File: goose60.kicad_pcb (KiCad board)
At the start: 2 copper layers, 285 x 94.6 mm, 179 parts, among them J1 Debugger, J2 USART, J3 SPI, P1 USB_C_Plug_USB2.0, SW1 SW_Push, SW10 SW_Push, SW11 SW_Push, SW14 SW_Push, SW15 SW_Push, SW16 SW_Push, SW18 SW_Push, SW2 SW_Push, SW20 SW_Push, SW21 SW_Push, SW22 SW_Push, SW23 SW_Push, SW24 SW_Push, SW25 SW_Push, SW26 SW_Push, SW27 SW_Push, SW28 SW_Push, SW29 SW_Push, SW3 SW_Push, SW30 SW_Push, SW31 SW_Push, SW32 SW_Push, SW35 SW_Push, SW36 SW_Push, SW37 SW_Push, SW38 SW_Push, SW39 SW_Push, SW40 SW_Push, SW41 SW_Push, SW42 SW_Push, SW43 SW_Push, SW44 SW_Push, SW45 SW_Push, SW46 SW_Push, SW47 SW_Push, SW48 SW_Push, SW49 SW_Push, SW5 SW_Push, SW50 SW_Push, SW51 SW_Push, SW52 SW_Push, SW53 SW_Push, SW54 SW_Push, SW56 SW_Push, SW58 SW_Push, SW59 SW_Push, SW60 SW_Push, SW61 SW_Push, SW62 SW_Push, SW65 SW_Push, SW66 SW_Push, SW67 SW_Push, SW68 SW_Push, SW69 SW_Push, SW7 SW_Push, SW71 SW_Push, SW73 SW_Push, SW74 SW_Push, SW75 SW_Push, SW76 SW_Push, SW78 SW_Push, SW79 SW_Push, SW80 SW_Push, SW82 SW_Push, SW84 SW_Push, SW86 SW_Push, SW9 SW_Push, U1 STM32F103CBTx, U2 LM317_SOT-223, X1 Crystal_GND24

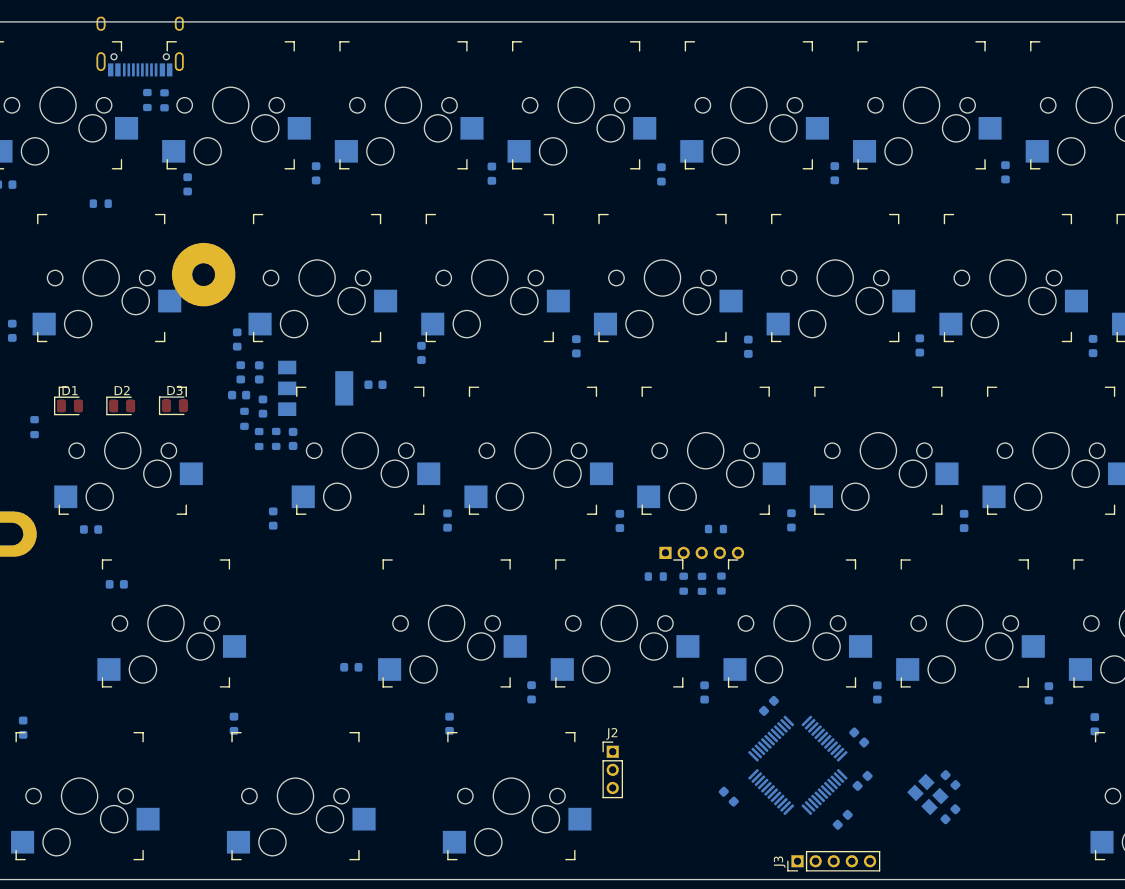
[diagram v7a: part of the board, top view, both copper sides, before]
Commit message: add res and fix rule check fail problom
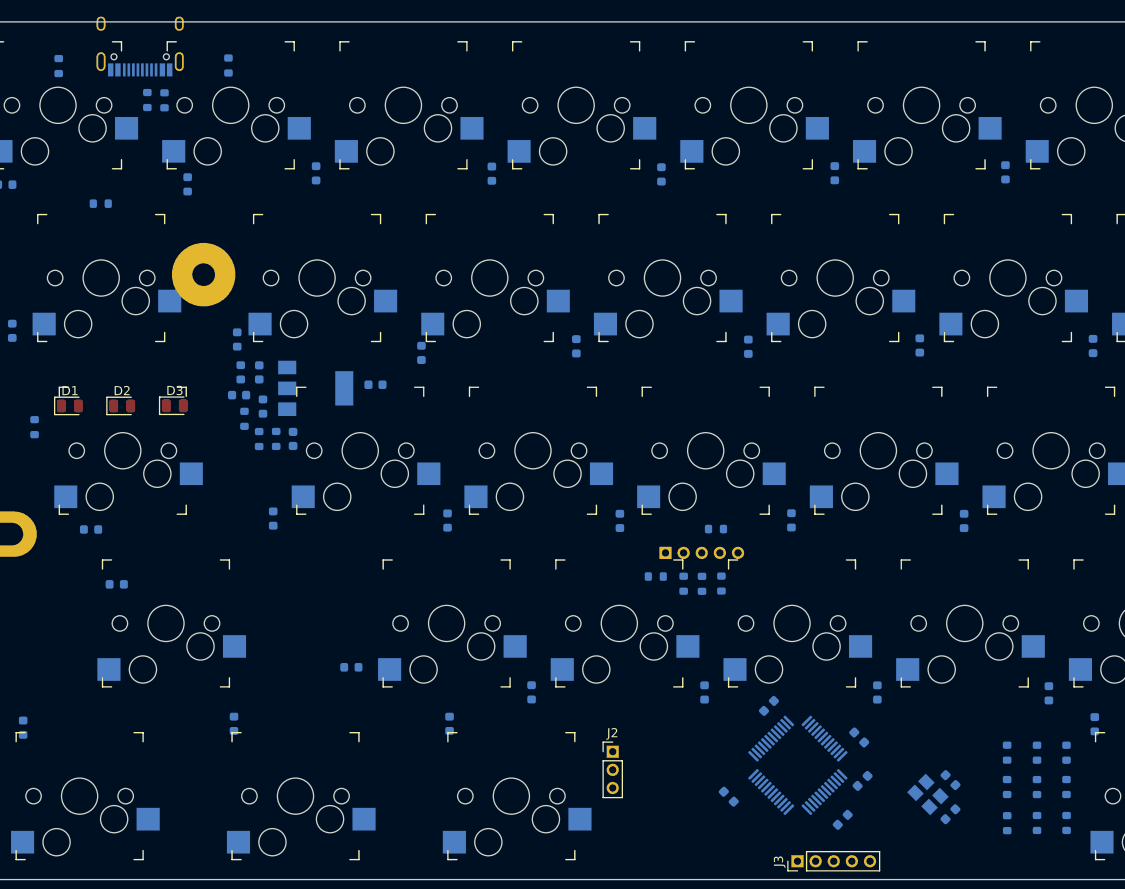
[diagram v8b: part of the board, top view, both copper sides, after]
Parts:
- added R15: 10K, Resistor_SMD:R_0603_1608Metric, B.Cu at (176.4, 145.8)
- added R16: 10K, Resistor_SMD:R_0603_1608Metric, B.Cu at (176.4, 149.6)
- added R17: 10K, Resistor_SMD:R_0603_1608Metric, B.Cu at (179.7, 145.8)
- added R18: 10K, Resistor_SMD:R_0603_1608Metric, B.Cu at (179.7, 149.6)
- added R19: 10K, Resistor_SMD:R_0603_1608Metric, B.Cu at (182.9, 145.8)
- added R20: 10K, Resistor_SMD:R_0603_1608Metric, B.Cu at (182.9, 149.6)
- added R21: 10K, Resistor_SMD:R_0603_1608Metric, B.Cu at (182.9, 153.6)
- added R22: 10K, Resistor_SMD:R_0603_1608Metric, B.Cu at (179.7, 153.6)
- added R23: 10K, Resistor_SMD:R_0603_1608Metric, B.Cu at (176.4, 153.6)
- added R24: 5.1K, Resistor_SMD:R_0603_1608Metric, B.Cu at (71.8, 70.1)
- added R25: 0, Resistor_SMD:R_0603_1608Metric, B.Cu at (90.5, 70.0)
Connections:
- net /col1 renamed col1
- net /col10 renamed col10
- net /col11 renamed col11
- net /col12 renamed col12
- net /col13 renamed col13
- net /col14 renamed col14
- net /col2 renamed col2
- net /col3 renamed col3
- net /col4 renamed col4
- net /col5 renamed col5
- net /col6 renamed col6
- net /col7 renamed col7
- net /col8 renamed col8
- net /col9 renamed col9
- net /row1 renamed row1
- net /row2 renamed row2
- net /row3 renamed row3
- net /row4 renamed row4
- net /row5 renamed row5
- P1 pad A5: unconnected-(P1-PadA5) -> Net-(P1-PadA5)
- P1 pad B5: unconnected-(P1-PadB5) -> Net-(P1-PadB5)
- U1 pad 10: unconnected-(U1-Pad10) -> PA0
- U1 pad 2: unconnected-(U1-Pad2) -> PC13
- U1 pad 29: unconnected-(U1-Pad29) -> PA8
- U1 pad 3: unconnected-(U1-Pad3) -> PC14
- U1 pad 38: unconnected-(U1-Pad38) -> PA15
- U1 pad 4: unconnected-(U1-Pad4) -> PC15
